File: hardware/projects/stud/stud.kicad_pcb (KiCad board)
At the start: 2 copper layers, 1 part, among them U2 TAC5242

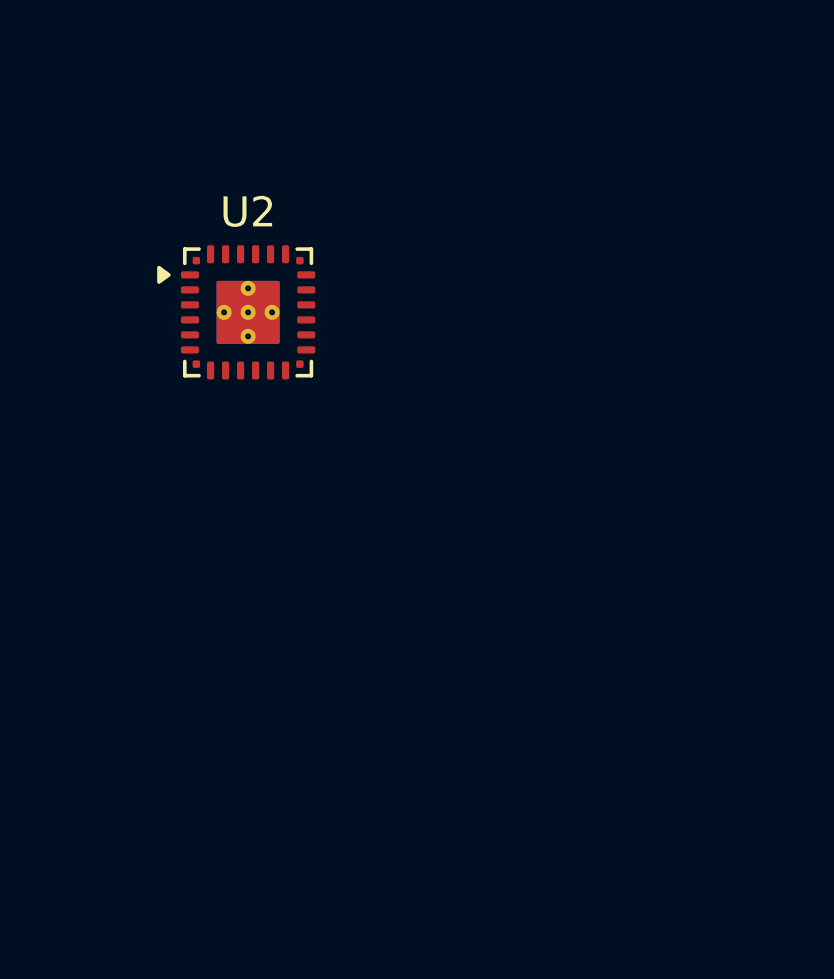
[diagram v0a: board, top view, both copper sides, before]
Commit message: add RA8M2, propose memory chip
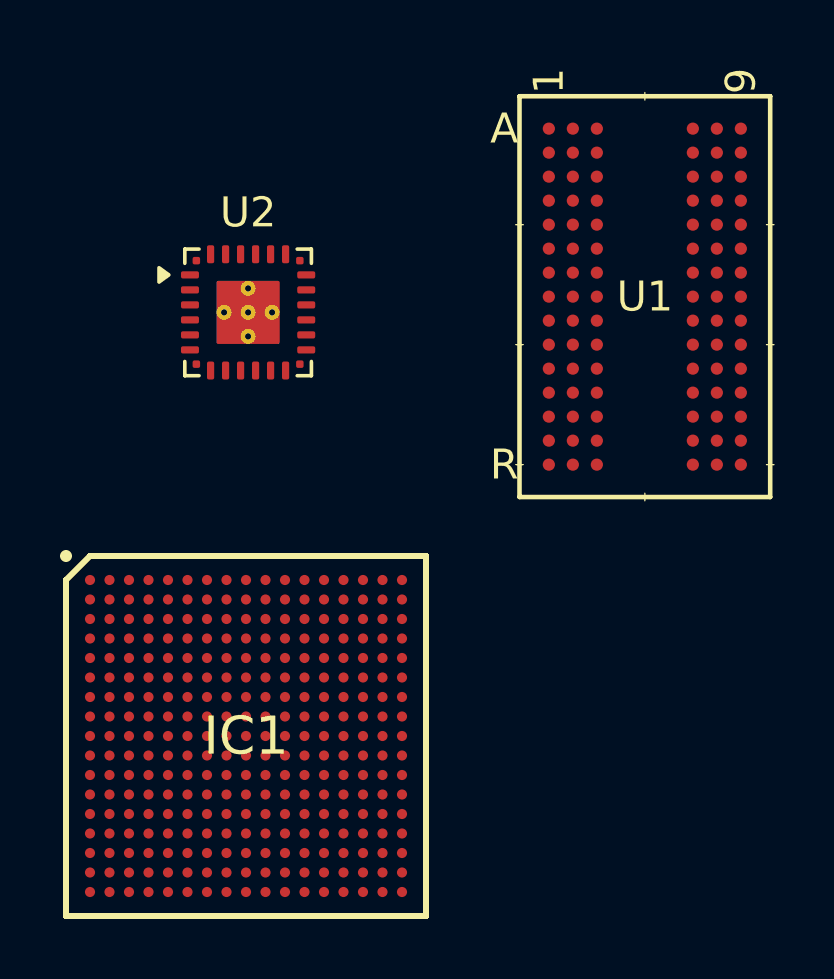
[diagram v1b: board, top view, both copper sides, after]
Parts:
- added IC1: R7KA8M2JFLCAC#UC0, vendor:BGA289C65P17X17_1200X1200X138, F.Cu at (134.0, 111.2)
- added U1: IS42VM32160E-75BLI, vendor:TFBGA-90_8X13_ISI, F.Cu at (147.3, 96.5)
